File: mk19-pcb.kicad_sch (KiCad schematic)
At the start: 96 parts, among them J1 Conn_01x03_Socket, J10 Conn_01x02_Socket, J11 Conn_01x02_Socket, J12 Conn_01x02_Socket, J2 Conn_01x03_Socket, J3 Conn_01x02_Socket, J4 Conn_01x02_Socket, J5 Conn_01x02_Socket, J6 Conn_01x02_Socket, J7 Conn_01x02_Socket, J8 Conn_01x04_Socket, J9 Conn_01x02_Socket, P1 FH26W-13S-0_3SHW(60), P10 FH26W-13S-0_3SHW(60), P11 FH26W-13S-0_3SHW(60), P2 FH26W-13S-0_3SHW(60), P3 FH26W-13S-0_3SHW(60), P4 FH26W-13S-0_3SHW(60), P5 FH26W-13S-0_3SHW(60), P6 FH26W-13S-0_3SHW(60), P7 FH26W-13S-0_3SHW(60), P8 FH26W-13S-0_3SHW(60), P9 FH26W-13S-0_3SHW(60), T1 Conn_01x01_Socket, T10 Conn_01x01_Socket, T2 Conn_01x01_Socket, T3 Conn_01x01_Socket, T4 Conn_01x01_Socket, T5 Conn_01x01_Socket, T6 Conn_01x01_Socket, T7 Conn_01x01_Socket, T8 Conn_01x01_Socket, T9 Conn_01x01_Socket, U1 AZC199-04S-MS, U10 8_01A0_008200, U2 1N4148W_C81598, U3 1N4148W_C81598, U4 1N4148W_C81598, U5 1N4148W_C81598, U6 1N4148W_C81598, U7 HC-FPC-05-10-16RLTAG, U8 ECT818001569, U9 8_01A0_008200

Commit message: all new features added, fixes implemented, ready to start arranging and routing
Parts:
- removed 5WAY1: Conn_01x06_Socket, Connector_JST:JST_EH_B6B-EH-A_1x06_P2.50mm_Vertical, symbol Connector:Conn_01x06_Socket
- removed G4, G5: Conn_01x01_Socket, Connector_Pin:Pin_D1.0mm_L10.0mm, symbol Connector:Conn_01x01_Socket
- added 5WAY1: Conn_01x08_Socket, Connector_JST:JST_EH_S8B-EH_1x08_P2.50mm_Horizontal, symbol Connector:Conn_01x08_Socket
- added C10, C11, C12, C7, C8, C9: CL31B105KBHNNNE, ct-kicad:C1206, symbol ct-kicad:CL31B105KBHNNNE
- added COL_JOIN2, COL_JOIN3: Conn_01x02_Socket, Connector_PinSocket_2.54mm:PinSocket_1x02_P2.54mm_Vertical, symbol Connector:Conn_01x02_Socket
- added LED1: 0805G_(Green), ct-kicad:LED0805-R-RD, symbol ct-kicad:0805G_(Green)
- added R10: 1206W4F1002T5E, ct-kicad:R1206, symbol ct-kicad:1206W4F1002T5E
- added R6, R7, R8: 4.7k, ct-kicad:R1206, symbol ct-kicad:1206W4F1002T5E
- added R9: 0402WGF2001TCE, ct-kicad:R0402, symbol ct-kicad:0402WGF2001TCE
- added U11: 8_01A0_008200, ct-kicad:FPC-SMD_8P-P0.50_8.01A0.008200, symbol ct-kicad:8_01A0_008200
- COL1, COL2, FAL1, FAL2, PWM1, ROW1, ROW2: footprint Connector_JST:JST_XH_B8B-XH-A_1x08_P2.50mm_Vertical -> Connector_JST:JST_EH_S8B-EH_1x08_P2.50mm_Horizontal
- COL_JOIN1: renamed from J3; footprint (none) -> Connector_PinSocket_2.54mm:PinSocket_1x02_P2.54mm_Vertical
- FAL_PINS1: renamed from J8; footprint (none) -> Connector_PinSocket_2.54mm:PinSocket_1x04_P2.54mm_Vertical
- J10, J11, J12, J4, J9: footprint (none) -> Connector_PinSocket_2.54mm:PinSocket_1x02_P2.54mm_Vertical
- R2, R3, R4, R5: footprint footprint:RES-ARRAY-SMD_0603-8P-L3.2-W1.6-BL -> ct-kicad:RES-ARRAY-SMD_0603-8P-L3.2-W1.6-BL
- SPLIT_HAND1: renamed from J2; footprint (none) -> Connector_PinSocket_2.54mm:PinSocket_1x03_P2.54mm_Vertical
- U10, U9: footprint footprint:FPC-SMD_8P-P0.50_8.01A0.008200 -> ct-kicad:FPC-SMD_8P-P0.50_8.01A0.008200
- VCC_BYPASS1: renamed from J1; footprint (none) -> Connector_PinSocket_2.54mm:PinSocket_1x03_P2.54mm_Vertical
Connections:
- net GPIO22 is gone; now on net GPIO6: AUDIO1.2 (Pin_2)
- net GPIO4 is gone; now on net COL_LATCH: PICO1.6 (GPIO4)
- net +3V3: now also C10.1, C11.1, C12.1, R10.2, R9.1, U11.2
- net COL_LATCH: now also COL_JOIN2.2 (Pin_2); no longer COL_JOIN1.2 (Pin_2), REG-COL1.12 (LATCH_CLOCK), REG-COL2.12 (LATCH_CLOCK)
- net GND: now also CYBOARD-MACRO1.17, CYBOARD-MACRO1.18, C10.2, C11.2, C12.2, C7.2, C8.2, C9.2, LED1.2 (K), R8.2, U11.1, U11.10, U11.9
- net SPI1_CLK: now also R8.1, U11.3
- net SPI1_MISO: now also COL_JOIN3.2 (Pin_2)
- net SPI1_MOSI: now also U11.4
- net VCC: now also C7.1, C8.1, C9.1
- net col0: now also R3.4; no longer R3.1
- net col1: now also R3.3; no longer R3.2
- net col10: now also R5.2; no longer R5.3
- net col11: now also R5.1; no longer R5.4
- net col12: now also R4.4; no longer R4.1
- net col13: now also R4.3; no longer R4.2
- net col14: now also R4.2; no longer R4.3
- net col15: now also R4.1; no longer R4.4
- net col2: now also R3.2; no longer R3.3
- net col3: now also R3.1; no longer R3.4
- net col4: now also R2.4; no longer R2.1
- net col5: now also R2.3; no longer R2.2
- net col6: now also R2.2; no longer R2.3
- net col7: now also R2.1; no longer R2.4
- net col8: now also R5.4; no longer R5.1
- net col9: now also R5.3; no longer R5.2
- net row5: now also 5WAY1.7 (Pin_7)
- net at U4.2 (A): now also 5WAY1.3 (Pin_3)
- net at U6.2 (A): now also 5WAY1.4 (Pin_4)
- net at U3.2 (A): now also 5WAY1.5 (Pin_5)
- net at U5.2 (A): now also 5WAY1.6 (Pin_6)
- net at U2.2 (A): now also 5WAY1.8 (Pin_8)
- new net: COL_JOIN1.2 (Pin_2), COL_JOIN2.1 (Pin_1), REG-COL1.12 (LATCH_CLOCK), REG-COL2.12 (LATCH_CLOCK)
- new net: LED1.1 (A), R9.2
- new net: 5WAY1.2 (Pin_2), R6.1
- new net: 5WAY1.1 (Pin_1), R7.1
- new net: COL_JOIN3.1 (Pin_1), R10.1
- new net SPARE_1: U11.5
- new net SPARE_2: U11.6
- new net SPARE_3: U11.7
- new net SPARE_4: U11.8
- new net rkjxt-a: R6.2
- new net rkjxt-b: R7.2
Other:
- note added: "Falcon button breakout"
- note added: "GC9A01 LCDs"
- note added: "LED power breakouts"
- note added: "Power LED"
- note removed: "LCD"
- moved on the sheet: AUDIO1, C2, C4, C5, C6, COL_CS_MOS1, COL_JOIN1, DBG1, FAL_PINS1, G2, G3, G6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

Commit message: feb16 work, almost ready to start running traces
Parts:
- removed G2, G3, G6, T1, T2, T3, T4, T7, T8: Conn_01x01_Socket, Connector_Pin:Pin_D1.0mm_L10.0mm, symbol Connector:Conn_01x01_Socket
- removed J5, J6: Conn_01x02_Socket, Connector_JST:JST_EH_B2B-EH-A_1x02_P2.50mm_Vertical, symbol Connector:Conn_01x02_Socket
- added GPIO1, PWR-OUT6: Conn_01x03_Socket, Connector_PinSocket_2.54mm:PinSocket_1x03_P2.54mm_Vertical, symbol Connector:Conn_01x03_Socket
- added J1, J2, PWR-EXT-IN1: Conn_01x02_Socket, Connector_JST:JST_EH_B2B-EH-A_1x02_P2.50mm_Vertical, symbol Connector:Conn_01x02_Socket
- renumbered COL_JOIN3 to MISO_PULL1
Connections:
- net GND: now also J1.1 (Pin_1), J2.1 (Pin_1), PWR-EXT-IN1.1 (Pin_1)
- net GPIO3: now also GPIO1.1 (Pin_1)
- net GPIO7: now also GPIO1.2 (Pin_2)
- net GPIO8: now also GPIO1.3 (Pin_3)
- net LED_3v3_DI: no longer PICO1.34 (GPIO28_ADC2)
- net VCC: now also PWR-OUT6.3 (Pin_3); no longer C7.1, C8.1, C9.1, J7.2 (Pin_2)
- net LED_DI_3.3V renamed LED_DI_3v3
- net LED_DI_3v3: now also PICO1.34 (GPIO28_ADC2)
- new net: PWR-EXT-IN1.2 (Pin_2), PWR-OUT6.1 (Pin_1)
- new net LED_5V: C7.1, C8.1, C9.1, J1.2 (Pin_2), J2.2 (Pin_2), J7.2 (Pin_2), PWR-OUT6.2 (Pin_2)
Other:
- note added: "LED external power input"
- note removed: "Breakouts"
- moved on the sheet: 5WAY1, ADC1, AUDIO1, C1, C10, C11, C12, C2, C3, C4, C5, C6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

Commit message: first draft done - needs work on led signal flow, silkscreen, falcon row-col thing.
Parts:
- removed GPIO1: Conn_01x03_Socket, Connector_PinSocket_2.54mm:PinSocket_1x03_P2.54mm_Vertical, symbol Connector:Conn_01x03_Socket
- removed J12: Conn_01x02_Socket, Connector_PinSocket_2.54mm:PinSocket_1x02_P2.54mm_Vertical, symbol Connector:Conn_01x02_Socket
- removed T5: Conn_01x01_Socket, Connector_Pin:Pin_D1.0mm_L10.0mm, symbol Connector:Conn_01x01_Socket
- J10, J11, J4, J9: footprint Connector_PinSocket_2.54mm:PinSocket_1x02_P2.54mm_Vertical -> Connector_JST:JST_EH_B2B-EH-A_1x02_P2.50mm_Vertical
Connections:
- net GPIO7 is gone; now on net rkjxt-a: PICO1.10 (GPIO7)
- net GPIO8 is gone; now on net rkjxt-b: PICO1.11 (GPIO8)
- net LED_3v3_DI is gone; now on net LED_DI_3v3: LED-LVL1.3 (A)
- net LED_SCREEN_DI: no longer J11.1 (Pin_1)
- net col0: now also COL1.8 (Pin_8); no longer COL1.1 (Pin_1)
- net col1: now also COL1.7 (Pin_7); no longer COL1.2 (Pin_2)
- net col2: now also COL1.6 (Pin_6); no longer COL1.3 (Pin_3)
- net col3: now also COL1.5 (Pin_5); no longer COL1.4 (Pin_4)
- net col4: now also COL1.4 (Pin_4); no longer COL1.5 (Pin_5)
- net col5: now also COL1.3 (Pin_3); no longer COL1.6 (Pin_6)
- net col6: now also COL1.2 (Pin_2); no longer COL1.7 (Pin_7)
- net col7: now also COL1.1 (Pin_1); no longer COL1.8 (Pin_8)
- net row0: now also ROW1.8 (Pin_8); no longer ROW1.1 (Pin_1)
- net row1: now also ROW1.7 (Pin_7); no longer ROW1.2 (Pin_2)
- net row2: now also ROW1.6 (Pin_6); no longer ROW1.3 (Pin_3)
- net row3: now also ROW1.5 (Pin_5); no longer ROW1.4 (Pin_4)
- net row4: now also ROW1.4 (Pin_4); no longer ROW1.5 (Pin_5)
- net row5: now also ROW1.3 (Pin_3); no longer ROW1.6 (Pin_6)
- net row6: now also ROW1.2 (Pin_2); no longer ROW1.7 (Pin_7)
- net row7: now also ROW1.1 (Pin_1); no longer ROW1.8 (Pin_8)
- net LED_EXTRA_DI: no longer names the net of J11.2 (Pin_2)
- net LED_EXT_DI renamed LED_SCREEN_DO
- net LED_SCREEN_DO: now also J11.1 (Pin_1)
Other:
- note added: "Indicators From screen, to extra"
- note removed: "GPIO breakout"
- note removed: "Indicators Extra"
- note removed: "Indicators Screen"

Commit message: ready for review
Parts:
- removed FAL_PINS1: Conn_01x04_Socket, Connector_PinSocket_2.54mm:PinSocket_1x04_P2.54mm_Vertical, symbol Connector:Conn_01x04_Socket
- removed T6, T9: Conn_01x01_Socket, Connector_Pin:Pin_D1.0mm_L10.0mm, symbol Connector:Conn_01x01_Socket
- added LOGO5: **REF, ct-kicad:mk19-qr-logo-12mm, symbol ct-kicad:mk19-qr-12mm
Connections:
- net LED_INDICATORS_DI is gone; now on net LED_SLATS_BIG_DI: FAL2.4 (Pin_4)
- net fal1-col is gone; now on net col6: FAL1.6 (Pin_6)
- net fal1-row is gone; now on net row4: FAL1.5 (Pin_5)
- net fal2-col is gone; now on net col7: FAL2.6 (Pin_6)
- net fal2-row is gone; now on net row4: FAL2.5 (Pin_5)
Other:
- note removed: "Falcon button breakout"

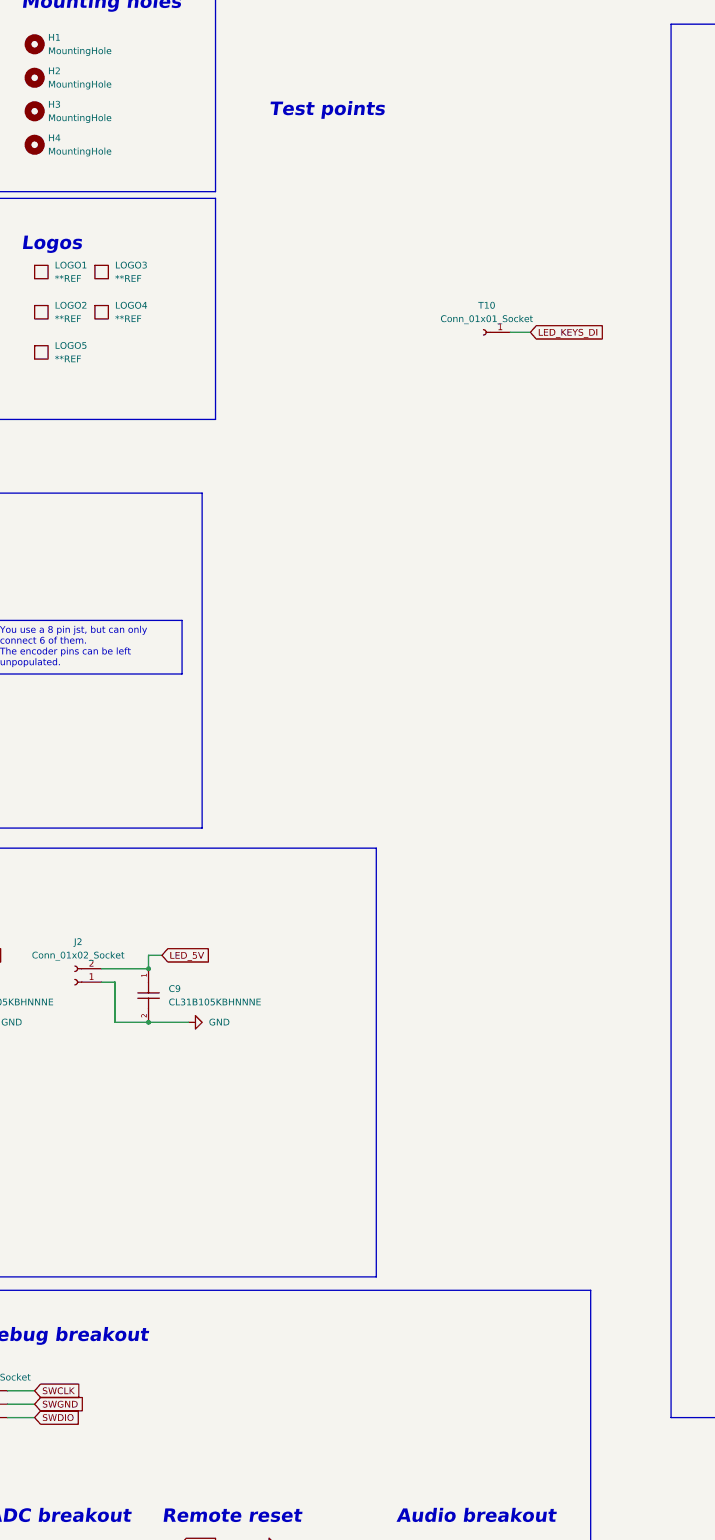
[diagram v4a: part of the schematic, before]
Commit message: missed cyboard branding, added a test pin for macro led DI
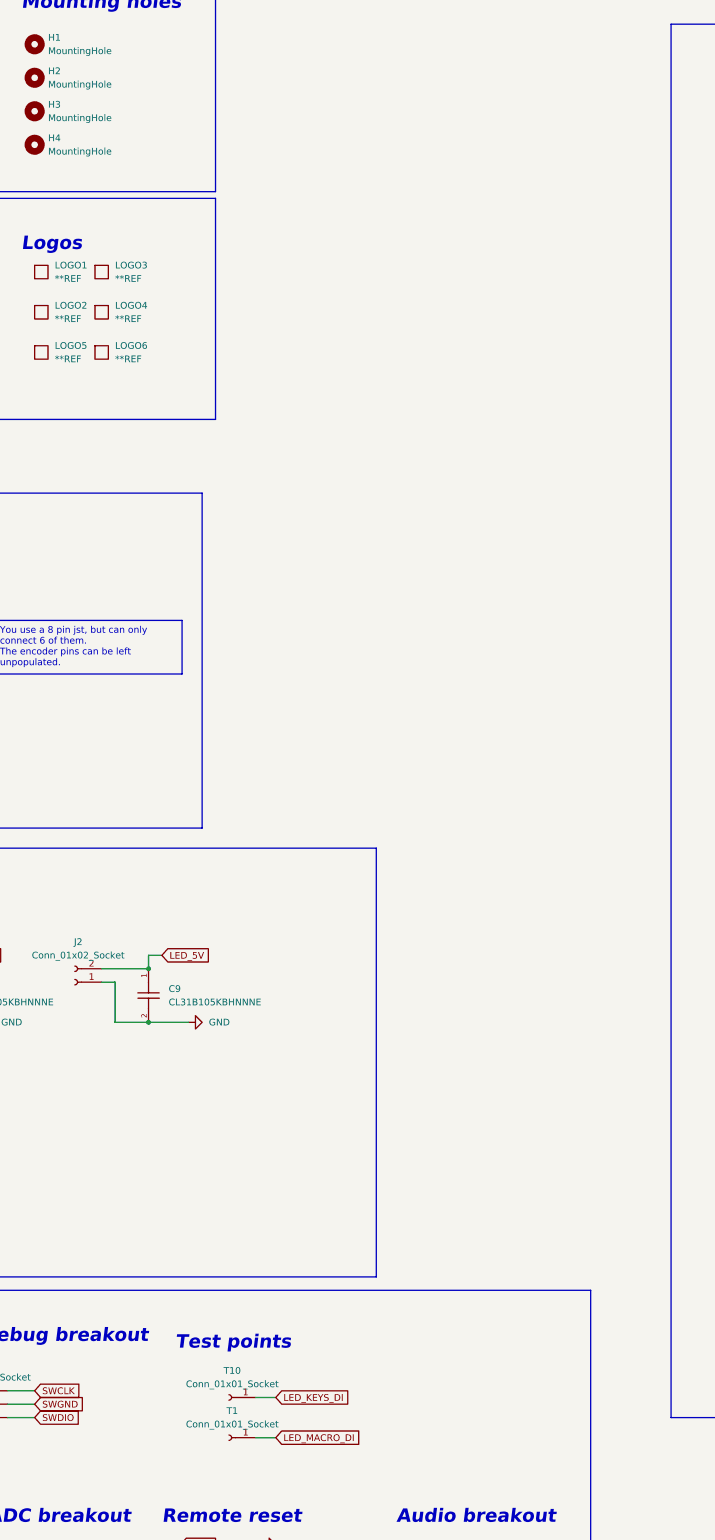
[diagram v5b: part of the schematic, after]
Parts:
- added LOGO6: **REF, ct-kicad:cyboard-logo-10mm, symbol ct-kicad:cyboard-logo-10mm
- added T1: Conn_01x01_Socket, Connector_Pin:Pin_D1.0mm_L10.0mm, symbol Connector:Conn_01x01_Socket
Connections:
- net LED_MACRO_DI: now also T1.1 (Pin_1)
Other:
- moved on the sheet: T10
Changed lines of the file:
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@@
     (stroke (width 0) (type default))
   )
-  (wire (pts (xy 574.04 82.55) (xy 577.85 82.55))
+  (wire (pts (xy 525.78 284.48) (xy 529.59 284.48))
     (stroke (width 0) (type default))
   )
@@
     (stroke (width 0) (type default))
   )
+  (wire (pts (xy 525.78 292.1) (xy 529.59 292.1))
+    (stroke (width 0) (type default))
+  )
   (wire (pts (xy 697.23 162.56) (xy 697.23 163.83))
     (stroke (width 0) (type default))
@@
     (effects (font (face "Futura") (size 2.54 2.54) (thickness 0.508) bold italic) (justify left bottom))
   )
-  (text "Test points" (at 528.32 41.91 0)
+  (text "Test points" (at 510.54 275.59 0)
     (effects (font (face "Futura") (size 2.54 2.54) (thickness 0.508) bold italic) (justify left bottom))
   )
@@
     )
   )
+  (global_label "LED_MACRO_DI" (shape input) (at 529.59 292.1 0) (fields_autoplaced)
+    (effects (font (size 1.27 1.27)) (justify left))
+    (property "Intersheetrefs" "${INTERSHEET_REFS}" (at 546.2428 292.1 0)
+      (effects (font (size 1.27 1.27)) (justify left) hide)
+    )
+  )
   (global_label "PMW_CS" (shape input) (at 400.05 146.05 0) (fields_autoplaced)
     (effects (font (size 1.27 1.27)) (justify left))
@@
     )
   )
-  (global_label "LED_KEYS_DI" (shape input) (at 577.85 82.55 0) (fields_autoplaced)
+  (global_label "LED_KEYS_DI" (shape input) (at 529.59 284.48 0) (fields_autoplaced)
     (effects (font (size 1.27 1.27)) (justify left))
-    (property "Intersheetrefs" "${INTERSHEET_REFS}" (at 592.8094 82.55 0)
+    (property "Intersheetrefs" "${INTERSHEET_REFS}" (at 544.5494 284.48 0)
       (effects (font (size 1.27 1.27)) (justify left) hide)
     )
@@
     )
   )
-  (symbol (lib_id "Connector:Conn_01x01_Socket") (at 568.96 82.55 180) (unit 1)
+  (symbol (lib_id "Connector:Conn_01x01_Socket") (at 520.7 284.48 180) (unit 1)
     (in_bom no) (on_board yes) (dnp no) (fields_autoplaced)
-    (property "Reference" "T10" (at 569.595 77.47 0)
+    (property "Reference" "T10" (at 521.335 279.4 0)
       (effects (font (size 1.27 1.27)))
     )
-    (property "Value" "Conn_01x01_Socket" (at 569.595 80.01 0)
+    (property "Value" "Conn_01x01_Socket" (at 521.335 281.94 0)
       (effects (font (size 1.27 1.27)))
     )
-    (property "Footprint" "Connector_Pin:Pin_D1.0mm_L10.0mm" (at 568.96 82.55 0)
+    (property "Footprint" "Connector_Pin:Pin_D1.0mm_L10.0mm" (at 520.7 284.48 0)
       (effects (font (size 1.27 1.27)) hide)
     )
-    (property "Datasheet" "~" (at 568.96 82.55 0)
+    (property "Datasheet" "~" (at 520.7 284.48 0)
       (effects (font (size 1.27 1.27)) hide)
     )
@@
     )
   )
+  (symbol (lib_id "ct-kicad:cyboard-logo-10mm") (at 496.57 86.36 0) (unit 1)
+    (in_bom no) (on_board yes) (dnp no) (fields_autoplaced)
+    (property "Reference" "LOGO6" (at 499.11 85.09 0)
+      (effects (font (size 1.27 1.27)) (justify left))
+    )
+    (property "Value" "**REF" (at 499.11 87.63 0)
+      (effects (font (size 1.27 1.27)) (justify left))
+    )
+    (property "Footprint" "ct-kicad:cyboard-logo-10mm" (at 496.57 86.36 0)
+      (effects (font (size 1.27 1.27)) hide)
+    )
+    (property "Datasheet" "" (at 496.57 86.36 0)
+      (effects (font (size 1.27 1.27)) hide)
+    )
+    (instances
+      (project "mk19-pcb"
+        (path "/2353ceae-84c1-4f16-856e-bae2658fe2c9"
+          (reference "LOGO6") (unit 1)
+        )
+      )
+    )
+  )
   (symbol (lib_id "power:GND") (at 345.44 81.28 270) (unit 1)
     (in_bom yes) (on_board yes) (dnp no) (fields_autoplaced)
@@
         )
       )
+    )
+  )
+  (symbol (lib_id "Connector:Conn_01x01_Socket") (at 520.7 292.1 180) (unit 1)
+    (in_bom no) (on_board yes) (dnp no) (fields_autoplaced)
+    (property "Reference" "T1" (at 521.335 287.02 0)
+      (effects (font (size 1.27 1.27)))
+    )
+    (property "Value" "Conn_01x01_Socket" (at 521.335 289.56 0)
+      (effects (font (size 1.27 1.27)))
+    )
+    (property "Footprint" "Connector_Pin:Pin_D1.0mm_L10.0mm" (at 520.7 292.1 0)
+      (effects (font (size 1.27 1.27)) hide)
+    )
+    (property "Datasheet" "~" (at 520.7 292.1 0)
+      (effects (font (size 1.27 1.27)) hide)
+    )
+    (pin "1")
+    (instances
+      (project "mk19-pcb"
+        (path "/2353ceae-84c1-4f16-856e-bae2658fe2c9"
+          (reference "T1") (unit 1)
+        )
+      )
